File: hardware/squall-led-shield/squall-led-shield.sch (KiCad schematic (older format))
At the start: 11 parts, among them J1 SQUALL_HEADER, Q1 Q_2NMOS

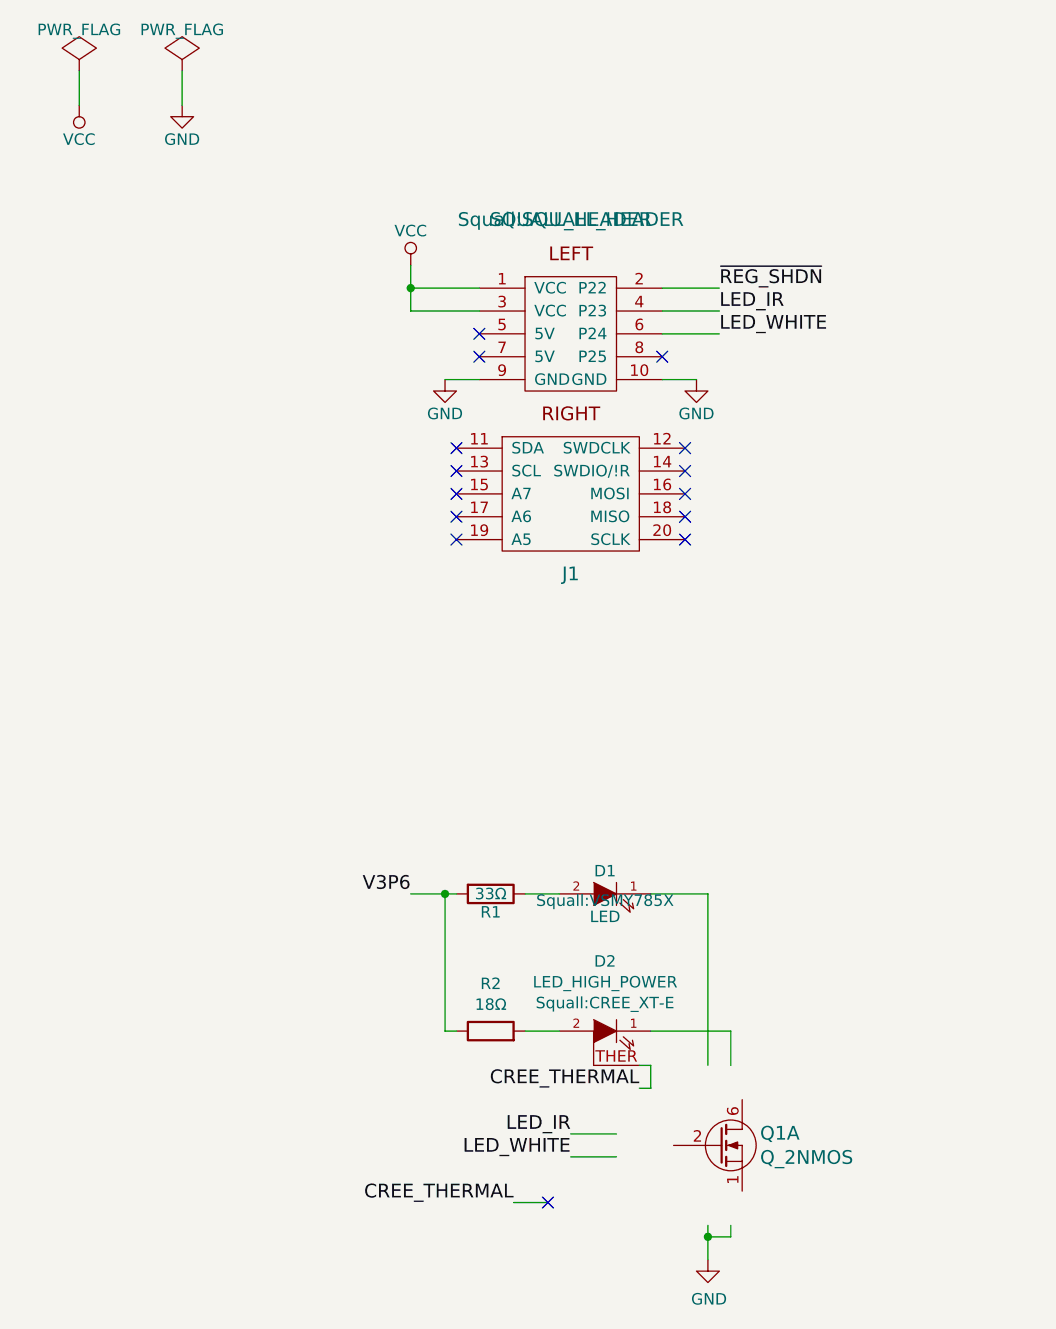
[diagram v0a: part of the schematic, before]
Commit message: WIP: Create proper nfet array component
As I come to see enlightenment, I see that this is one where KiCad
and Eagle both have it half right, but I think KiCad is closer to
being able to be full right.
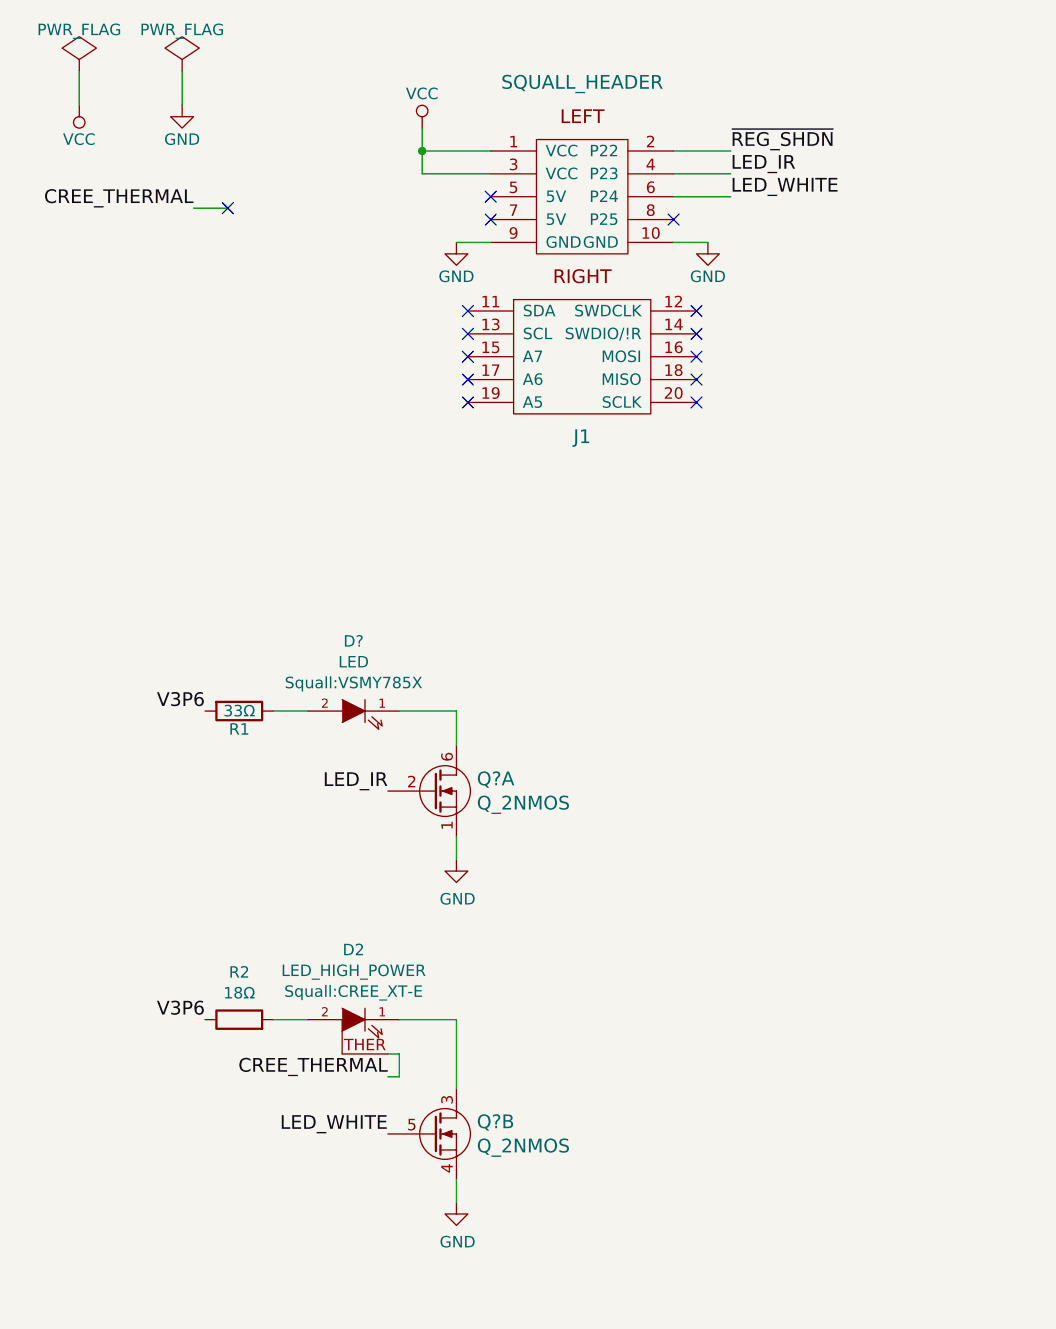
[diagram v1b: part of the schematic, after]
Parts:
- removed D1: LED, Squall:VSMY785X, symbol LED
- removed Q1: Q_2NMOS, TO_SOT_Packages_SMD:SC-70-6, symbol Q_2NMOS
- added D?: LED, Squall:VSMY785X, symbol LED
- added Q? (x2): Q_2NMOS, symbol Q_2NMOS
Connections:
- wire segments 42 -> 36
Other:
- moved on the sheet: D2, J1, R1, R2

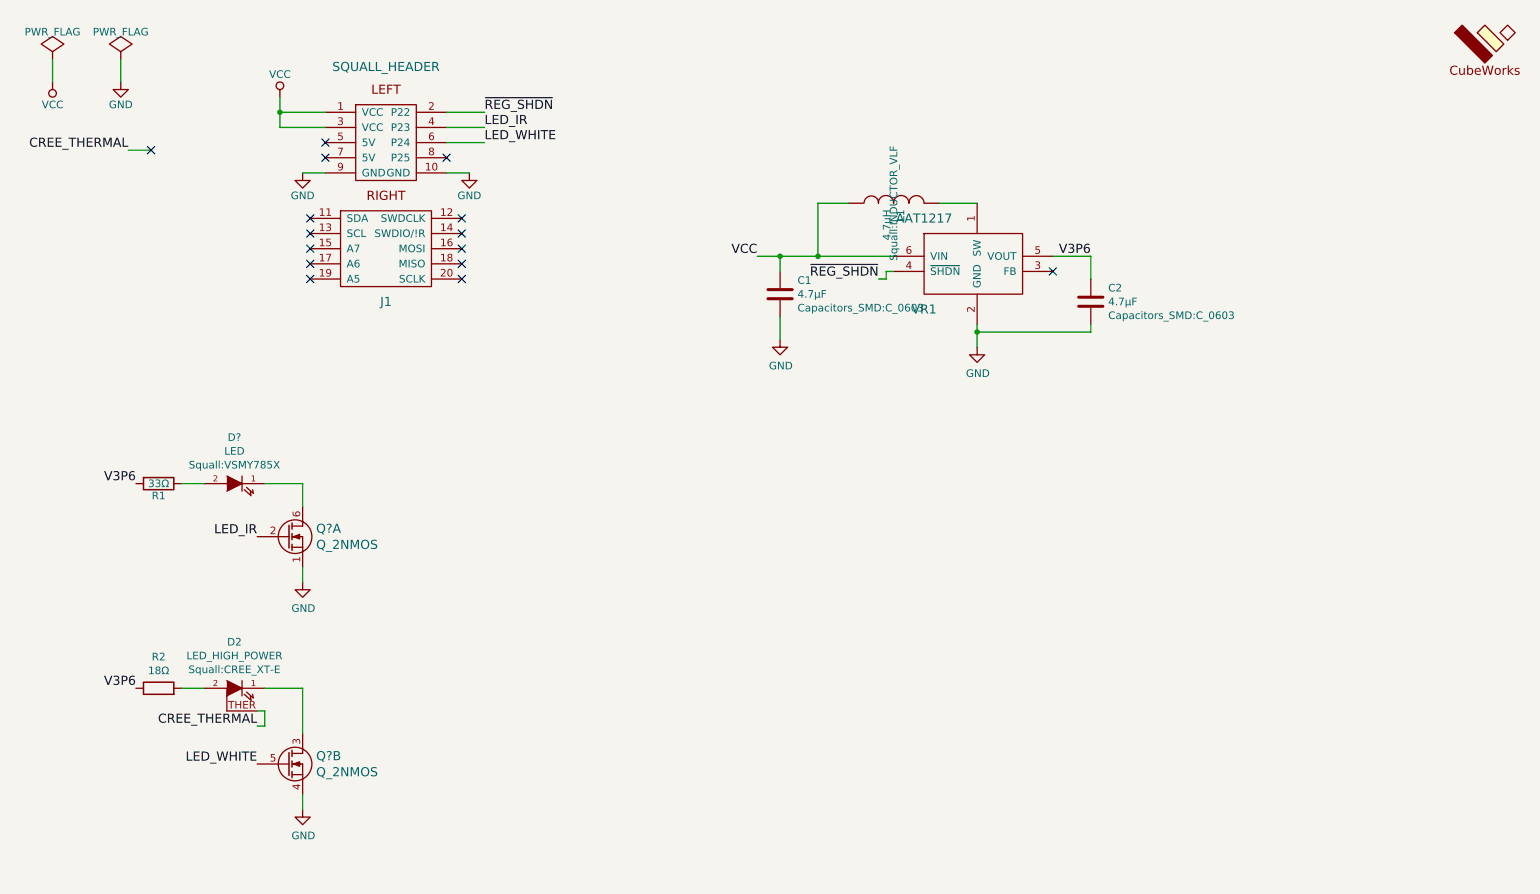
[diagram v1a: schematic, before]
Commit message: WIP: VREG -> 5V
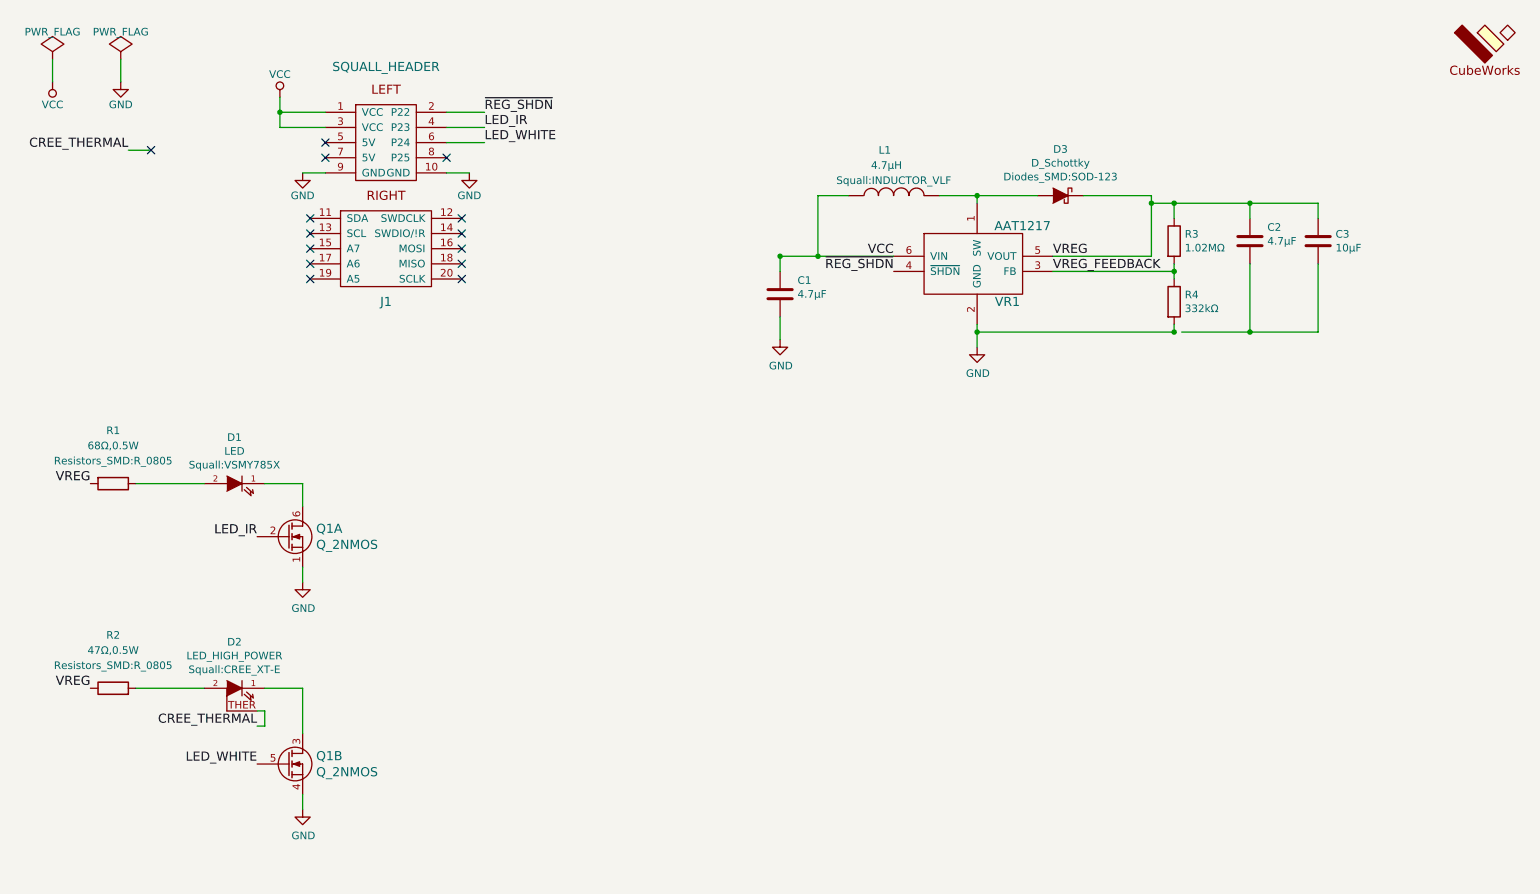
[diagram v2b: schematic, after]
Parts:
- added C3: 10µF, Capacitors_SMD:C_0603, symbol C
- added D3: D_Schottky, Diodes_SMD:SOD-123, symbol D_Schottky
- added R3: 1.02MΩ, Resistors_SMD:R_0603, symbol R
- added R4: 332kΩ, Resistors_SMD:R_0603, symbol R
- R1: value 33Ω -> 68Ω,0.5W; footprint Resistors_SMD:R_0603 -> Resistors_SMD:R_0805
- R2: value 18Ω -> 47Ω,0.5W; footprint Resistors_SMD:R_0603 -> Resistors_SMD:R_0805
- gave numbers to parts that had none: 2
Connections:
- net GND: now also R4.2; no longer C2.2
- net at L1.2, VR1.1 (SW): now also D3.2 (A)
- net VREG_FEEDBACK: now reaches VR1.3 (FB)
- net VREG_FEEDBACK: now also R3.2, R4.1
- net V3P6 renamed VREG
- net VREG: now also C3.1, D3.1 (K), R3.1
- new net: C2.2, C3.2
- no-connect marks 15 -> 14
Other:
- moved on the sheet: C2, L1, R1, R2

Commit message: WIP: Fresh routing
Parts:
- Q1: footprint (none) -> TO_SOT_Packages_SMD:SC-70-6
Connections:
- net GND: now also C2.2, C3.2
- net SQUALL_5V: now reaches J1.5 (5V)
- net SQUALL_5V: now also J1.7 (5V)
- net VREG_SW: now reaches D3.2 (A), L1.2, VR1.1 (SW)
- no-connect marks 14 -> 12
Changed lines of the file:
@@
 	1    0    0    -1
 $EndComp
-NoConn ~ 2550 1350
-NoConn ~ 2550 1450
 NoConn ~ 3350 1450
 NoConn ~ 2450 1850
@@
 U 1 1 579646C6
 P 2300 3950
-F 0 "Q1" H 2489 4003 60  0000 L CNN
-F 1 "Q_2NMOS" H 2489 3897 60  0000 L CNN
-F 2 "" H 2675 4050 60  0001 C CNN
+F 0 "Q1" H 2489 4056 60  0000 L CNN
+F 1 "Q_2NMOS" H 2489 3950 60  0000 L CNN
+F 2 "TO_SOT_Packages_SMD:SC-70-6" H 2489 3844 60  0000 L CNN
 F 3 "" H 2675 4050 60  0001 C CNN
 	1    2300 3950
@@
 	8650 2600 8650 2150
 Wire Wire Line
-	8200 2600 8650 2600
+	8150 2600 8650 2600
 Wire Wire Line
 	8650 2600 9100 2600
@@
 	7550 1700 8000 1700
 Connection ~ 8000 1750
+Text Label 2550 1450 2    60   ~ 0
+SQUALL_5V
+Text Label 2550 1350 2    60   ~ 0
+SQUALL_5V
+Text Label 6650 1700 0    60   ~ 0
+VREG_SW
 $EndSCHEMATC

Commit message: Add Block M logo
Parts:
- added _2: BLOCK_M, Logos:BLOCK_M_SOLID_100MIL, symbol BLOCK_M
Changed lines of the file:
@@
 LIBS:valves
 LIBS:squall
+LIBS:logos
 LIBS:squall-led-shield-cache
 EELAYER 25 0
@@
 $EndComp
 $Comp
-L VCC #PWR01
+L VCC #PWR3
 U 1 1 579162D4
 P 2250 1050
-F 0 "#PWR01" H 2250 900 50  0001 C CNN
+F 0 "#PWR3" H 2250 900 50  0001 C CNN
 F 1 "VCC" H 2250 1200 50  0000 C CNN
 F 2 "" H 2250 1050 50  0000 C CNN
@@
 $EndComp
 $Comp
-L GND #PWR02
+L GND #PWR4
 U 1 1 57916308
 P 2400 1550
-F 0 "#PWR02" H 2400 1300 50  0001 C CNN
+F 0 "#PWR4" H 2400 1300 50  0001 C CNN
 F 1 "GND" H 2400 1400 50  0000 C CNN
 F 2 "" H 2400 1550 50  0000 C CNN
@@
 $EndComp
 $Comp
-L GND #PWR03
+L GND #PWR7
 U 1 1 57916322
 P 3500 1550
-F 0 "#PWR03" H 3500 1300 50  0001 C CNN
+F 0 "#PWR7" H 3500 1300 50  0001 C CNN
 F 1 "GND" H 3500 1400 50  0000 C CNN
 F 2 "" H 3500 1550 50  0000 C CNN
@@
 $EndComp
 $Comp
-L GND #PWR04
+L GND #PWR9
 U 1 1 57929427
 P 6850 2700
-F 0 "#PWR04" H 6850 2450 50  0001 C CNN
+F 0 "#PWR9" H 6850 2450 50  0001 C CNN
 F 1 "GND" H 6855 2527 50  0000 C CNN
 F 2 "" H 6850 2700 50  0000 C CNN
@@
 $EndComp
 $Comp
-L GND #PWR05
+L GND #PWR8
 U 1 1 57929808
 P 5550 2650
-F 0 "#PWR05" H 5550 2400 50  0001 C CNN
+F 0 "#PWR8" H 5550 2400 50  0001 C CNN
 F 1 "GND" H 5555 2477 50  0000 C CNN
 F 2 "" H 5550 2650 50  0000 C CNN
@@
 $EndComp
 $Comp
-L PWR_FLAG #FLG06
+L PWR_FLAG #FLG1
 U 1 1 57916600
 P 750 800
-F 0 "#FLG06" H 750 895 50  0001 C CNN
+F 0 "#FLG1" H 750 895 50  0001 C CNN
 F 1 "PWR_FLAG" H 750 980 50  0000 C CNN
 F 2 "" H 750 800 50  0000 C CNN
@@
 $EndComp
 $Comp
-L VCC #PWR07
+L VCC #PWR1
 U 1 1 57916658
 P 750 950
-F 0 "#PWR07" H 750 800 50  0001 C CNN
+F 0 "#PWR1" H 750 800 50  0001 C CNN
 F 1 "VCC" H 750 1100 50  0000 C CNN
 F 2 "" H 750 950 50  0000 C CNN
@@
 $EndComp
 $Comp
-L PWR_FLAG #FLG08
+L PWR_FLAG #FLG2
 U 1 1 5791661C
 P 1200 800
-F 0 "#FLG08" H 1200 895 50  0001 C CNN
+F 0 "#FLG2" H 1200 895 50  0001 C CNN
 F 1 "PWR_FLAG" H 1200 980 50  0000 C CNN
 F 2 "" H 1200 800 50  0000 C CNN
@@
 $EndComp
 $Comp
-L GND #PWR09
+L GND #PWR2
 U 1 1 5791663C
 P 1200 950
-F 0 "#PWR09" H 1200 700 50  0001 C CNN
+F 0 "#PWR2" H 1200 700 50  0001 C CNN
 F 1 "GND" H 1200 800 50  0000 C CNN
 F 2 "" H 1200 950 50  0000 C CNN
@@
 $EndComp
 $Comp
-L GND #PWR010
+L GND #PWR5
 U 1 1 57965F53
 P 2400 4250
-F 0 "#PWR010" H 2400 4000 50  0001 C CNN
+F 0 "#PWR5" H 2400 4000 50  0001 C CNN
 F 1 "GND" H 2405 4077 50  0000 C CNN
 F 2 "" H 2400 4250 50  0000 C CNN
@@
 $EndComp
 $Comp
-L GND #PWR011
+L GND #PWR6
 U 1 1 57965F88
 P 2400 5750
-F 0 "#PWR011" H 2400 5500 50  0001 C CNN
+F 0 "#PWR6" H 2400 5500 50  0001 C CNN
 F 1 "GND" H 2405 5577 50  0000 C CNN
 F 2 "" H 2400 5750 50  0000 C CNN
@@
 	8150 1750 8150 1850
 Wire Wire Line
-	8000 1750 8150 1750
-Wire Wire Line
-	8150 1750 8650 1750
-Wire Wire Line
-	8650 1750 9100 1750
-Wire Wire Line
-	8000 1700 8000 1750
-Wire Wire Line
-	8000 1750 8000 2100
+	8000 1750 9100 1750
+Wire Wire Line
+	8000 1700 8000 2100
 Wire Wire Line
 	8000 2100 7350 2100
@@
 	7350 2200 8150 2200
 Wire Wire Line
-	8150 2150 8150 2200
-Wire Wire Line
-	8150 2200 8150 2250
+	8150 2150 8150 2250
 Wire Wire Line
 	6850 1700 6850 1750
 Wire Wire Line
-	6600 1700 6850 1700
-Wire Wire Line
-	6850 1700 7250 1700
+	6600 1700 7250 1700
 Wire Wire Line
 	2400 5650 2400 5750
@@
 	5550 2100 5550 2200
 Wire Wire Line
-	5550 2100 5800 2100
-Wire Wire Line
-	5800 2100 6300 2100
+	5550 2100 6300 2100
 Wire Wire Line
 	5550 2650 5550 2500
@@
 	8650 2600 8650 2150
 Wire Wire Line
-	8150 2600 8650 2600
-Wire Wire Line
-	8650 2600 9100 2600
-Wire Wire Line
-	6850 2600 8150 2600
-Wire Wire Line
-	6850 2550 6850 2600
-Wire Wire Line
-	6850 2600 6850 2700
+	6850 2600 9100 2600
+Wire Wire Line
+	6850 2550 6850 2700
 Connection ~ 2250 1150
 Wire Wire Line
@@
 	2250 1250 2550 1250
 Wire Wire Line
-	2250 1050 2250 1150
-Wire Wire Line
-	2250 1150 2250 1250
+	2250 1050 2250 1250
 Wire Wire Line
 	3350 1550 3500 1550
@@
 Text Label 6650 1700 0    60   ~ 0
 VREG_SW
+$Comp
+L BLOCK_M _2
+U 1 1 5797B5E9
+P 9700 650
+F 0 "_2" H 9700 425 60  0001 C CNN
+F 1 "BLOCK_M" H 9700 800 60  0001 C CNN
+F 2 "Logos:BLOCK_M_SOLID_100MIL" H 9700 800 60  0001 C CNN
+F 3 "" H 9700 800 60  0001 C CNN
+	1    9700 650
+	1    0    0    -1
+$EndComp
 $EndSCHEMATC

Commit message: WIP: Add programming header
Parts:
- added J2: TC2030, connector:TC2030-IDC-NL, symbol TC2030
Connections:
- net GND: now also J2.5 (GND)
- net VCC: now also J2.1 (VCC)
- net ~REG_SHDN: now also J1.8 (P25); no longer J1.2 (P22)
- net SWDCLK: now reaches J1.12 (SWDCLK)
- net SWDCLK: now also J2.4 (SWDCLK)
- net SWDIO/~RESET: now reaches J1.14 (SWDIO/!R)
- net SWDIO/~RESET: now also J2.2 (SWDIO)
- new net P22: J1.2 (P22)
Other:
- moved on the sheet: C1, C2, C3, D1, D2, D3, J1, L1, Q1A, Q1B, R1, R2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
